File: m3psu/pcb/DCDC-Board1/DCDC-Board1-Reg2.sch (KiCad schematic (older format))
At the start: 38 parts

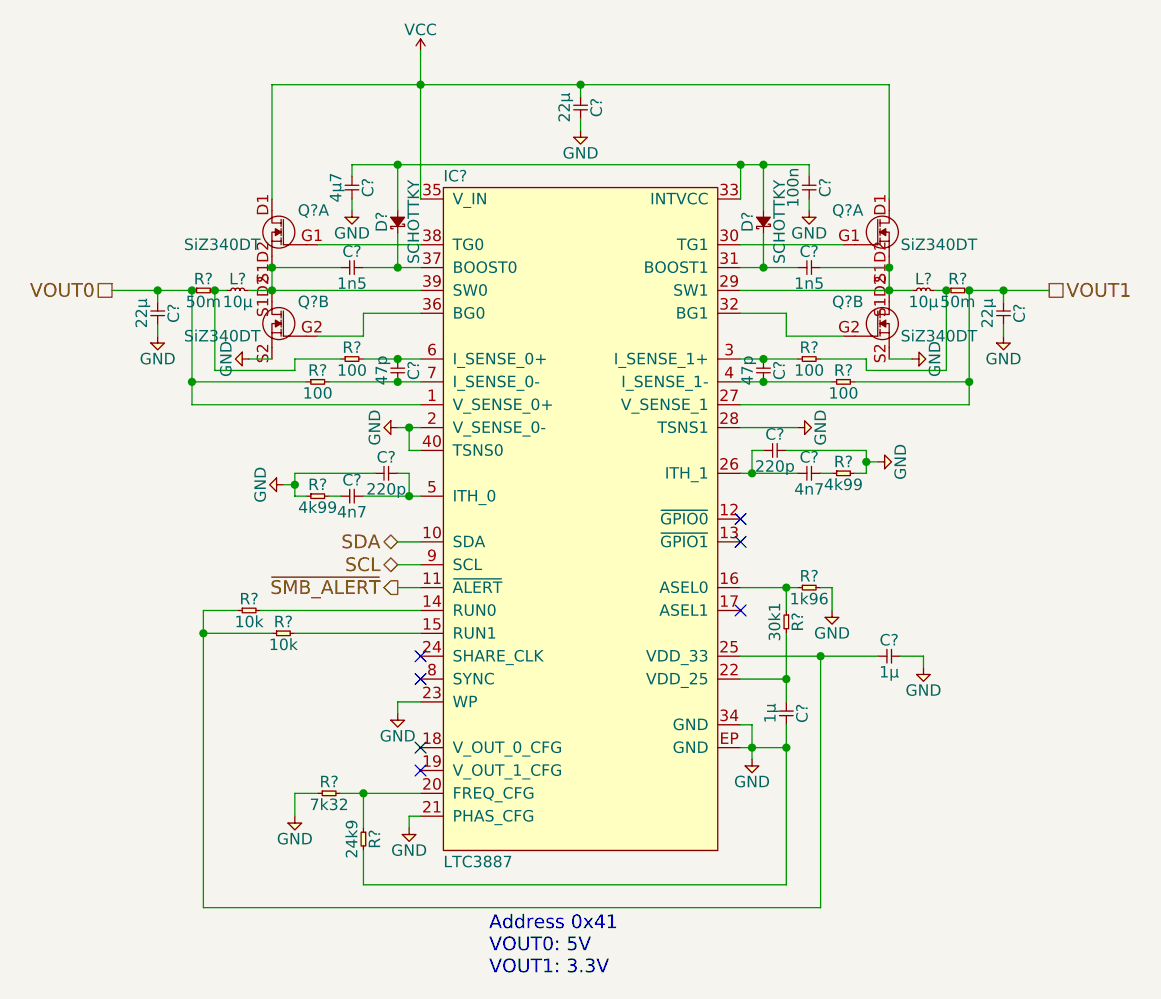
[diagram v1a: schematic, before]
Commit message: create DCDC1/2/3 from prototype
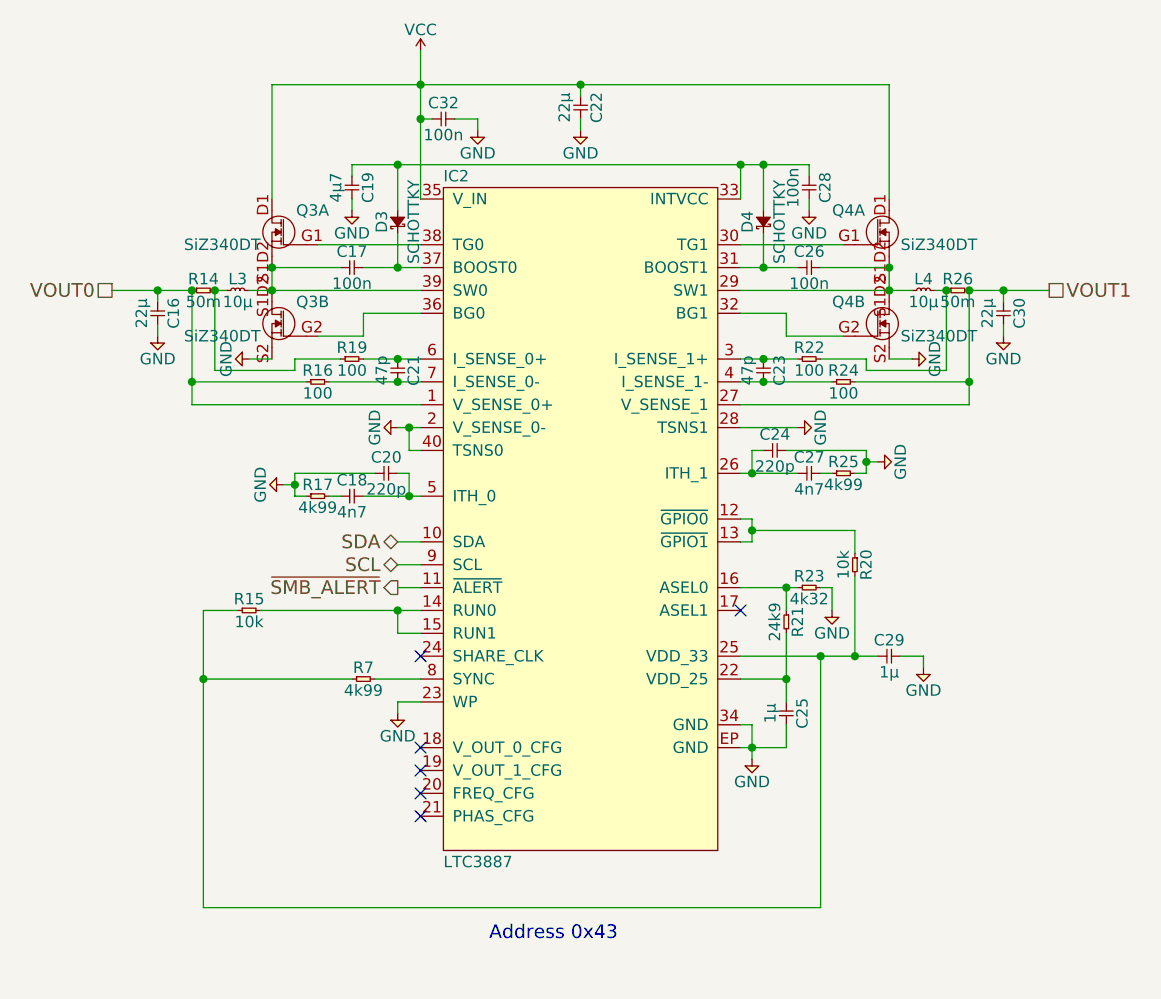
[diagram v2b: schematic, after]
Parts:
- removed C? (x2): 1n5, agg:0402, symbol C
- removed C?: 4µ7, agg:0603, symbol C
- removed C? (x3): 22µ, agg:0805, symbol C
- removed C? (x2): 47p, agg:0402, symbol C
- removed C? (x2): 1µ, agg:0402, symbol C
- removed C?: 100n, agg:0402, symbol C
- removed C? (x2): 4n7, agg:0402, symbol C
- removed C? (x2): 220p, agg:0402, symbol C
- removed D? (x2): SCHOTTKY, agg:0603-LED, symbol SCHOTTKY
- removed IC?: LTC3887, agg:QFN-40-EP-LTC-UJ, symbol LTC3887
- removed L? (x2): 10µ, agg:TYS5040, symbol L
- removed Q? (x4): SiZ340DT, agg:PowerPair3x3, symbol SiZ340DT
- removed R? (x2): 50m, agg:0603, symbol R
- removed R? (x4): 100, agg:0402, symbol R
- removed R?: 24k9, agg:0402, symbol R
- removed R?: 7k32, agg:0402, symbol R
- removed R?: 1k96, agg:0402, symbol R
- removed R?: 30k1, agg:0402, symbol R
- removed R? (x2): 4k99, agg:0402, symbol R
- removed R? (x2): 10k, agg:0402, symbol R
- added C16, C22, C30: 22µ, agg:0805, symbol C
- added C17, C26, C28, C32: 100n, agg:0402, symbol C
- added C18, C27: 4n7, agg:0402, symbol C
- added C19: 4µ7, agg:0402, symbol C
- added C20, C24: 220p, agg:0402, symbol C
- added C21, C23: 47p, agg:0402, symbol C
- added C25, C29: 1µ, agg:0402, symbol C
- added D3, D4: SCHOTTKY, agg:0603-LED, symbol SCHOTTKY
- added IC2: LTC3887, agg:QFN-40-EP-LTC-UJ, symbol LTC3887
- added L3, L4: 10µ, agg:TYS5040, symbol L
- added Q3, Q4: SiZ340DT, agg:PowerPair3x3, symbol SiZ340DT
- added R14, R26: 50m, agg:0603, symbol R
- added R15, R20: 10k, agg:0402, symbol R
- added R16, R19, R22, R24: 100, agg:0402, symbol R
- added R17, R25, R7: 4k99, agg:0402, symbol R
- added R21: 24k9, agg:0402, symbol R
- added R23: 4k32, agg:0402, symbol R
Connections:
- net GND: now also C16.2, C19.2, C20.1, C22.2, C24.2, C25.2, C28.2, C29.2, C30.2, C32.2, IC2.2 (V_SENSE_0-), IC2.23 (WP), IC2.28 (TSNS1), IC2.34 (GND), IC2.40 (TSNS0), IC2.EP (GND), Q3.S2, Q4.S2, R17.1, R23.2, R25.2
- net SCL: now also IC2.9 (SCL)
- net SDA: now also IC2.10 (SDA)
- net VCC: now also C22.1, C32.1, IC2.35 (V_IN), Q3.D1 (S1D2), Q4.D1 (S1D2)
- net VOUT0: now also C16.1, IC2.1 (V_SENSE_0+), R14.1, R16.1
- net VOUT1: now also C30.1, IC2.27 (V_SENSE_1), R24.2, R26.2
- net ~SMB_ALERT: now also IC2.11 (~ALERT)
- new net: IC2.12 (~GPIO0), IC2.13 (~GPIO1), R20.1
- new net: IC2.14 (RUN0), IC2.15 (RUN1), R15.2
- new net: IC2.16 (ASEL0), R21.1, R23.1
- new net: C25.1, IC2.22 (VDD_25), R21.2
- new net: C29.1, IC2.25 (VDD_33), R15.1, R20.2, R7.1
- new net: C24.1, C27.1, IC2.26 (ITH_1)
- new net: C26.2, IC2.29 (SW1), L4.1, Q4.S1D2, Q4.S1D2
- new net: C23.1, IC2.3 (I_SENSE_1+), R22.1
- new net: IC2.30 (TG1), Q4.G1
- new net: C26.1, D4.1, IC2.31 (BOOST1)
- new net: IC2.32 (BG1), Q4.G2
- new net: C19.1, C28.1, D3.2, D4.2, IC2.33 (INTVCC)
- new net: IC2.36 (BG0), Q3.G2
- new net: C17.2, D3.1, IC2.37 (BOOST0)
- new net: IC2.38 (TG0), Q3.G1
- new net: C17.1, IC2.39 (SW0), L3.2, Q3.S1D2, Q3.S1D2
- new net: C23.2, IC2.4 (I_SENSE_1-), R24.1
- new net: C18.2, C20.2, IC2.5 (ITH_0)
- new net: C21.1, IC2.6 (I_SENSE_0+), R19.2
- new net: C21.2, IC2.7 (I_SENSE_0-), R16.2
- new net: IC2.8 (SYNC), R7.2
- new net: L4.2, R22.2, R26.1
- new net: L3.1, R14.2, R19.1
- new net: C27.2, R25.1
- new net: C18.1, R17.2
- no-connect marks 7 -> 6
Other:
- note added: "Address 0x43"
- note removed: "Address 0x41\nVOUT0: 5V\nVOUT1: 3.3V"

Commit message: update DCDC address setting resistors due to making DCDC2 with DCDC1's resistors (intentionally)
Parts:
- R23: value 4k32 -> 7k32
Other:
- note added: "Address 0x45"
- note removed: "Address 0x43"
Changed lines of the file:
@@
 P 6800 4200
 F 0 "R23" H 6850 4250 50  0000 C CNN
-F 1 "4k32" H 6850 4150 50  0000 C CNN
+F 1 "7k32" H 6850 4150 50  0000 C CNN
 F 2 "agg:0402" H 6800 4200 50  0001 C CNN
 F 3 "" H 6800 4200 50  0001 C CNN
@@
 ~SMB_ALERT
 Text Notes 5450 5750 0    60   ~ 0
-Address 0x43
+Address 0x45
 Wire Wire Line
 	5050 4700 5150 4700
